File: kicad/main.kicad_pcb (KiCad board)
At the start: 2 copper layers, 198.1 x 99.1 mm, 66 parts, among them J1 Jack-DC, J12 I2C1, J14 LCD_Conn, J15 VIA_A, J2 UART, J3 Data, J4 PWR, J5 uSD, J6 VIA_B, J7 IO~{EN}_{[3..7]}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

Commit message: WIP: V16 GAL stuff
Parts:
- removed J6: VIA_B, Connector_PinHeader_2.54mm:PinHeader_1x04_P2.54mm_Vertical
- J2: footprint Connector_PinHeader_2.54mm:PinHeader_1x04_P2.54mm_Horizontal -> Connector_PinHeader_2.54mm:PinHeader_1x04_P2.54mm_Vertical
- J7: value IO~{EN}_{[3..7]} -> IO~{EN}_{[3..4]}; footprint Connector_PinHeader_2.54mm:PinHeader_1x05_P2.54mm_Vertical -> Connector_PinHeader_2.54mm:PinHeader_1x02_P2.54mm_Vertical
- moved R10 71.5 mm to (121.9, 61.0), turned to 180 degrees
- moved R11 68.6 mm to (121.9, 66.0), turned to 180 degrees
- moved C8 64.4 mm to (101.2, 113.5), turned to 90 degrees
- moved D3 29.0 mm to (190.5, 94.0)
- moved ROM1 27.4 mm to (57.6, 115.4), turned to 90 degrees
- moved J3 24.1 mm to (165.1, 106.7)
- moved X2 17.0 mm to (27.9, 78.7), turned to 90 degrees
- moved J4 10.5 mm to (182.9, 96.5)
- moved J7 5.68 mm to (165.1, 94.0)
- moved U4 5.08 mm to (176.5, 39.4)
- moved Y1 5.08 mm to (176.1, 34.0)
- moved J8 3.59 mm to (139.7, 94.0)
- moved C3 3.59 mm to (167.6, 77.5)
- moved IO1 3.59 mm to (154.9, 81.3)
- moved J9 2.54 mm to (139.7, 106.7)
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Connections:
- IO1 pad 10: IO~{EN}_{5} -> unconnected-(IO1-O5-Pad10)
- IO1 pad 7: IO~{EN}_{7} -> unconnected-(IO1-O7-Pad7)
- IO1 pad 9: IO~{EN}_{6} -> unconnected-(IO1-O6-Pad9)
- U6 pad 9: unconnected-(U6-I9-Pad9) -> ~{RES}
- VIA1 pad 17: Net-(J6-Pin_3) -> unconnected-(VIA1-PB7-Pad17)
- VIA1 pad 18: Net-(J6-Pin_4) -> unconnected-(VIA1-CB1-Pad18)
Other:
- board text added: "IO~EN~[3..4]"
- board text added: "by Andrew Dunai & 6502.org community"
- board text added: "m6502 SBC"
- board text removed: "65ad02"
- board text removed: "IO~EN~[2..7]"
- board text removed: "VIA_B"
- board text removed: "by and3rson & 6502.org community"

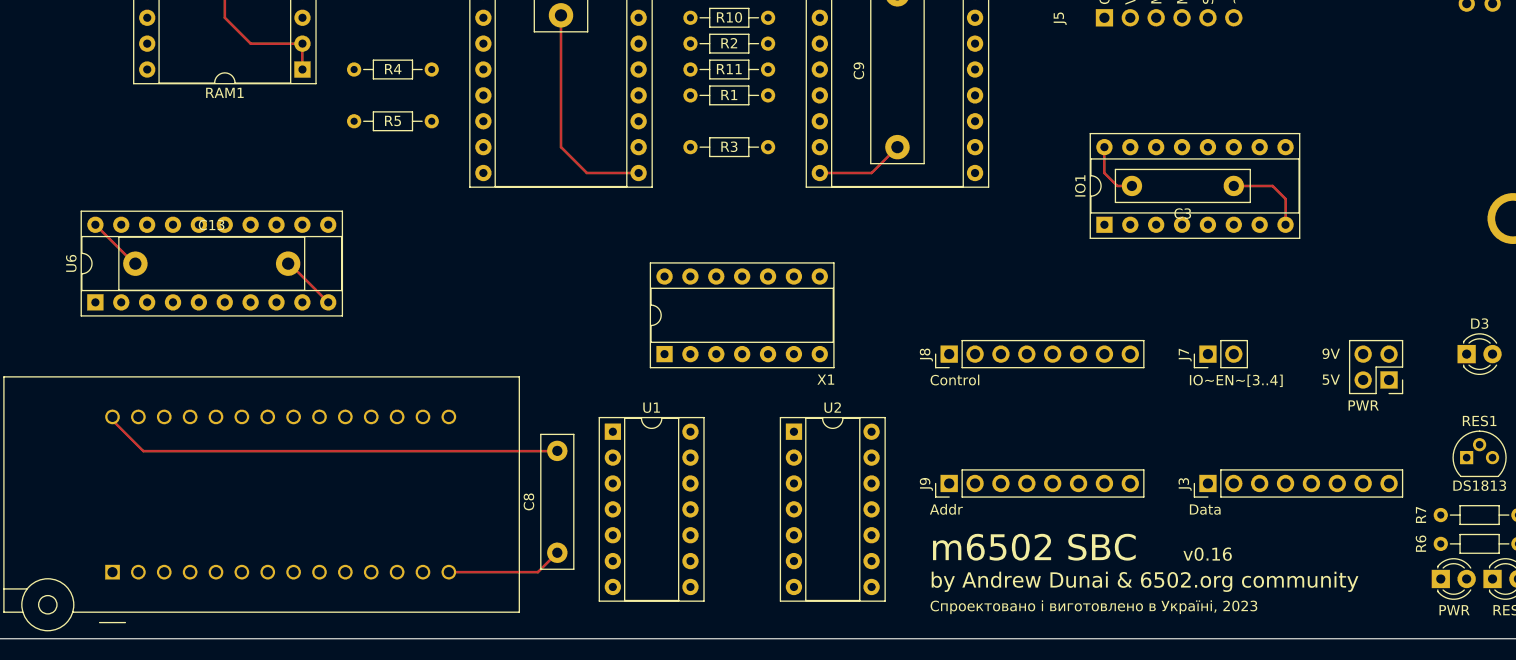
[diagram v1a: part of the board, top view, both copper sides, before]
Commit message: Replace address decoder & r/w qualifier with GAL
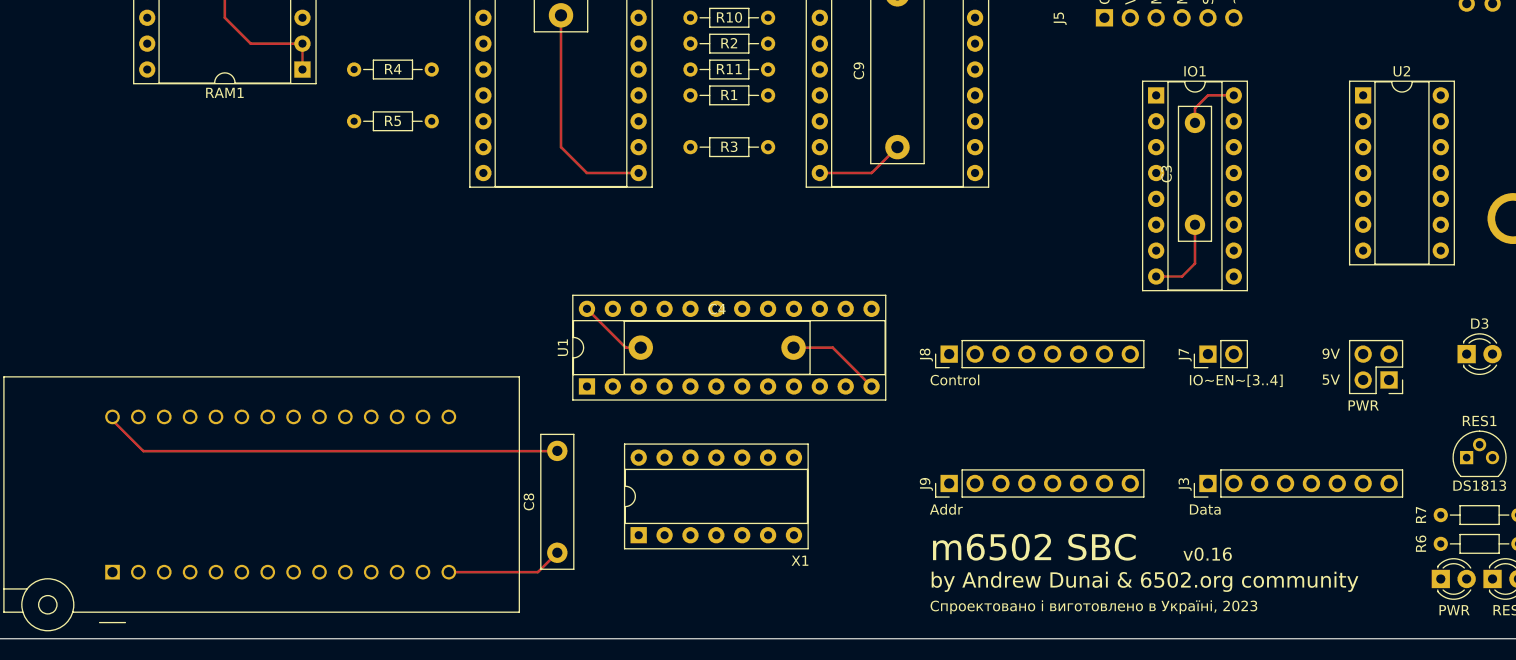
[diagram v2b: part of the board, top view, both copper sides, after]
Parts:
- removed C13: 0.1uF, Capacitor_THT:C_Rect_L18.0mm_W5.0mm_P15.00mm_FKS3_FKP3
- removed U6: GAL16V8, Package_DIP:DIP-20_W7.62mm_Socket
- added C4: 0.1uF, Capacitor_THT:C_Rect_L18.0mm_W5.0mm_P15.00mm_FKS3_FKP3, F.Cu at (109.4, 93.3)
- U1: value 74HC00 -> GAL20V8; footprint Package_DIP:DIP-14_W7.62mm_Socket -> Package_DIP:DIP-24_W7.62mm_Socket
- moved U2 64.9 mm to (180.3, 68.6)
- moved X1 18.0 mm to (109.2, 111.8)
- moved IO1 13.7 mm to (160.0, 68.6), turned to 0 degrees
- moved C3 5.39 mm to (163.8, 81.3), turned to 90 degrees
- moved U1 5.12 mm to (104.1, 97.2), turned to 90 degrees
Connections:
- IO1 pad 4: A_{13} -> GND
- IO1 pad 5: Net-(IO1-E2) -> IO~{EN}
- IO1 pad 6: A_{12} -> +5V
- U1 pad 1: A_{13} -> CLK
- U1 pad 10: A_{15} -> unconnected-(U1-I-Pad10)
- U1 pad 11: Net-(IO1-E2) -> unconnected-(U1-I-Pad11)
- U1 pad 12: A_{14} -> GND
- U1 pad 13: A_{15} -> GND
- U1 pad 14: +5V -> unconnected-(U1-I-Pad14)
- U1 pad 2: A_{14} -> unconnected-(U1-I-Pad2)
- U1 pad 3: Net-(U1-Pad3) -> LCD~{EN}
- U1 pad 4: Net-(U1-Pad3) -> ~{RES}
- U1 pad 5: A_{14} -> A_{12}
- U1 pad 6: Net-(U1-Pad6) -> A_{13}
- U1 pad 7: GND -> A_{14}
- U1 pad 8: ROM~{EN} -> A_{15}
- U1 pad 9: Net-(U1-Pad6) -> R~{W}
- U2 pad 1: R~{W} -> ~{RES}
- U2 pad 10: R~{W} -> (no net)
- U2 pad 11: Net-(R7-Pad1) -> (no net)
- U2 pad 12: ~{RES} -> (no net)
- U2 pad 13: ~{RES} -> (no net)
- U2 pad 2: R~{W} -> ~{RES}
- U2 pad 3: Net-(U2-Pad3) -> Net-(R7-Pad1)
- U2 pad 4: Net-(U2-Pad3) -> (no net)
- U2 pad 5: Ф2 -> (no net)
- U2 pad 6: ~{WD} -> (no net)
- U2 pad 8: ~{RD} -> (no net)
- U2 pad 9: Ф2 -> (no net)
- X1 pad 8: Net-(U6-I1/CLK) -> CLK
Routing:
- net GND: track 114.0 -> 117.7 mm
- net +5V: track 108.0 -> 109.3 mm

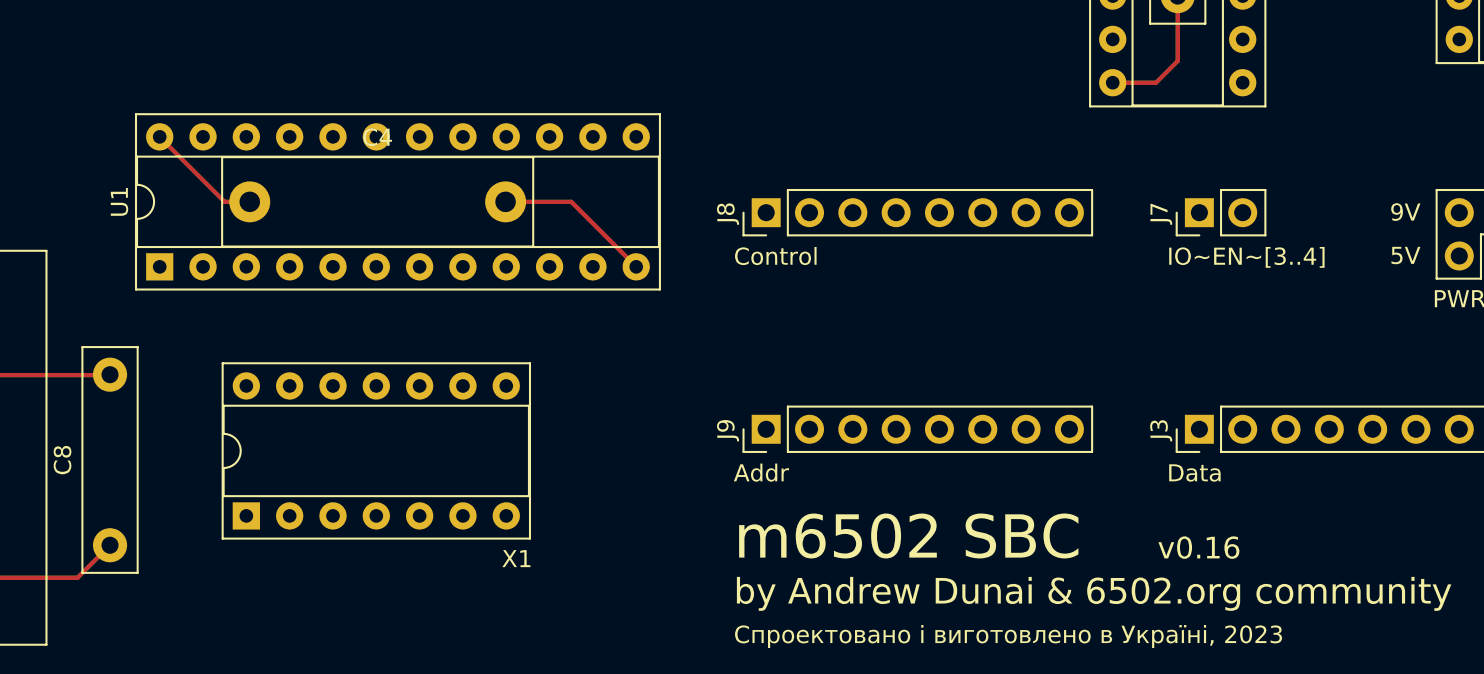
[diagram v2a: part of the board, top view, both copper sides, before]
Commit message: Replace GAL20V8 with GAL(ATF)16V8
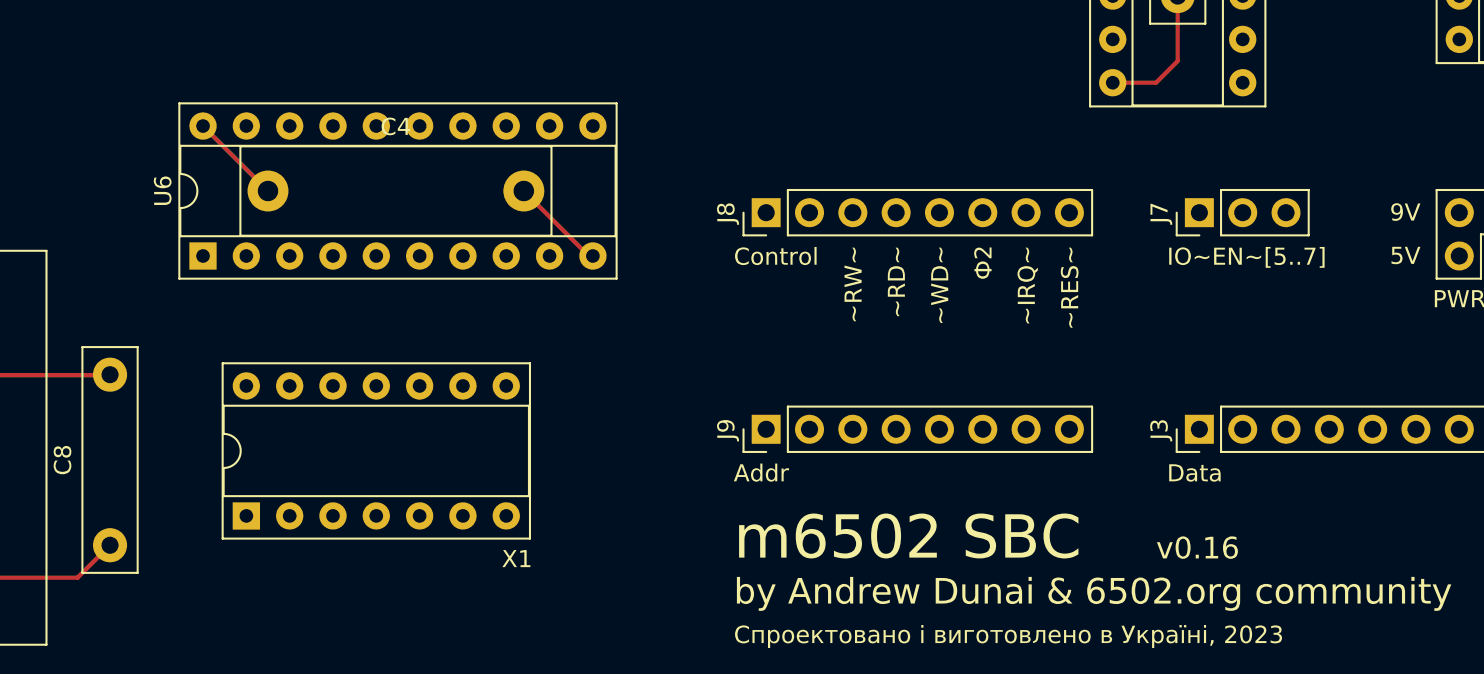
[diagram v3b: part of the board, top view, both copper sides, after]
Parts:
- removed U1: GAL20V8, Package_DIP:DIP-24_W7.62mm_Socket
- added U6: ATF16V8B-15PU, Package_DIP:DIP-20_W7.62mm_Socket, F.Cu at (106.7, 96.5)
- J7: value IO~{EN}_{[3..4]} -> IO~{EN}_{[5..7]}; footprint Connector_PinHeader_2.54mm:PinHeader_1x02_P2.54mm_Vertical -> Connector_PinHeader_2.54mm:PinHeader_1x03_P2.54mm_Vertical
- moved C4 1.24 mm to (110.5, 92.7)
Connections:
- IO1 pad 10: unconnected-(IO1-O5-Pad10) -> IO~{EN}_{5}
- IO1 pad 11: IO~{EN}_{4} -> SID~{EN}
- IO1 pad 12: IO~{EN}_{3} -> unconnected-(IO1-O3-Pad12)
- IO1 pad 7: unconnected-(IO1-O7-Pad7) -> IO~{EN}_{7}
- IO1 pad 9: unconnected-(IO1-O6-Pad9) -> IO~{EN}_{6}
- J7 pad 1: IO~{EN}_{3} -> IO~{EN}_{5}
- J7 pad 2: IO~{EN}_{4} -> IO~{EN}_{6}
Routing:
- net GND: track 117.7 -> 114.1 mm
- net +5V: track 109.3 -> 107.8 mm
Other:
- board text added: "IO~EN~[5..7]"
- board text added: "~IRQ~"
- board text added: "~RD~"
- board text added: "~RES~"
- board text added: "~RW~"
- board text added: "~WD~"
- board text added: "Ф2"
- board text removed: "IO~EN~[3..4]"

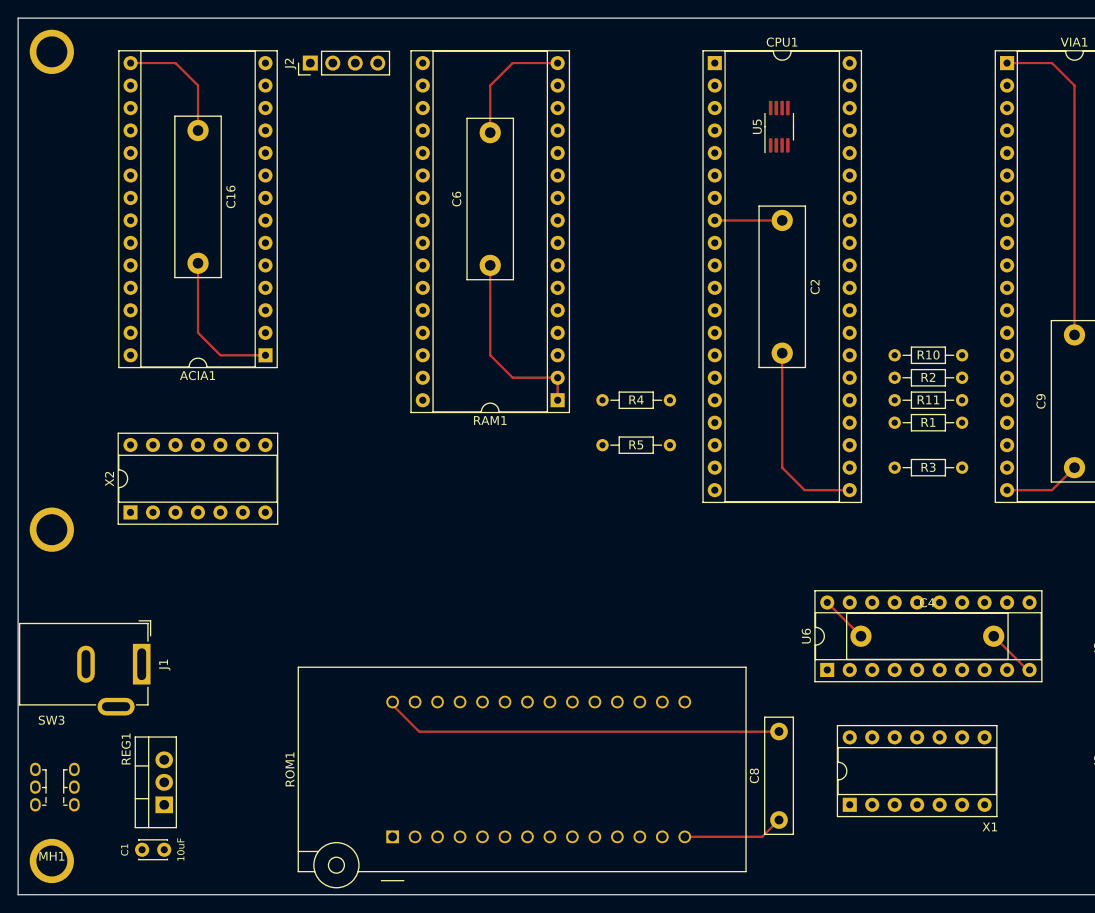
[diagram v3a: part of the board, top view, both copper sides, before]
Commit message: Move power socket to top, move GAL down a bit
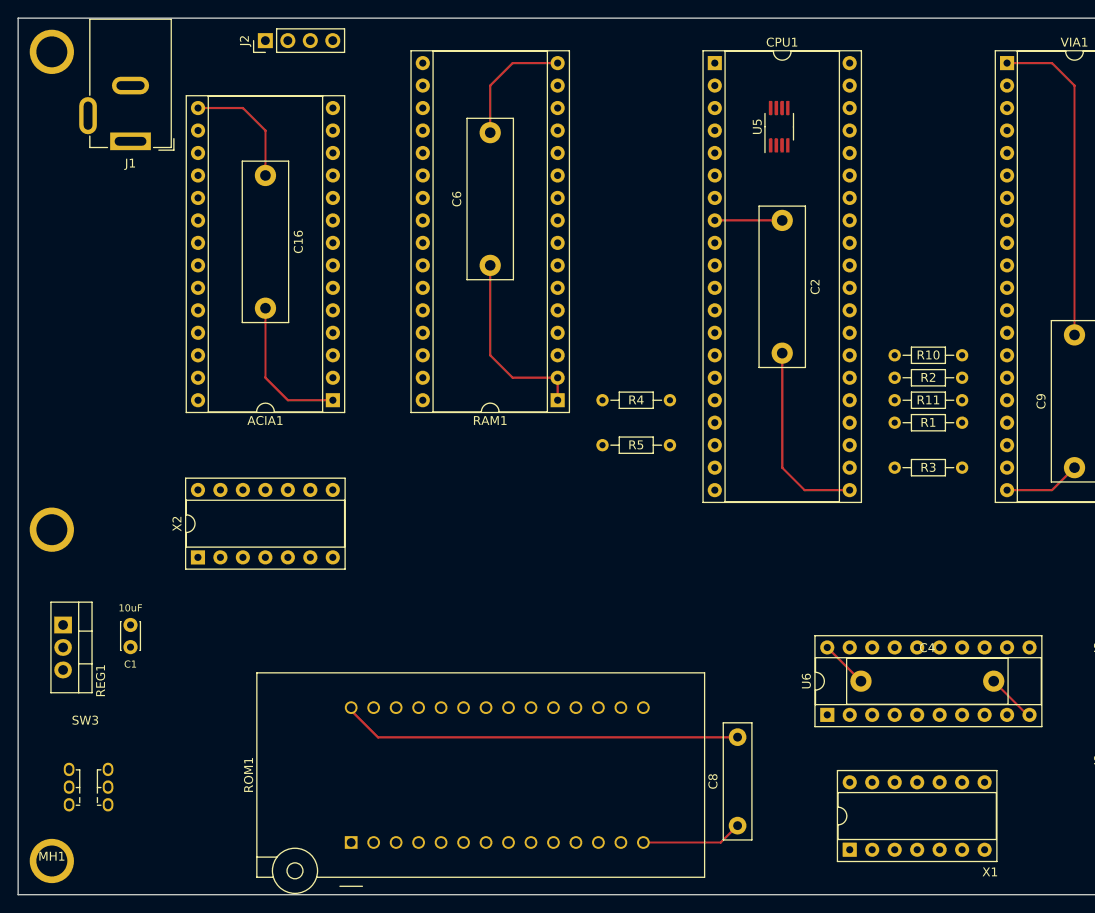
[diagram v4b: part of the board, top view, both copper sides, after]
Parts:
- moved J1 59.1 mm to (27.9, 36.8), turned to 180 degrees
- moved C1 25.7 mm to (27.9, 91.4), turned to -90 degrees
- moved REG1 23.3 mm to (20.3, 91.4), turned to -90 degrees
- moved ACIA1 9.16 mm to (50.8, 66.0)
- moved X2 9.16 mm to (35.6, 83.8)
- moved C16 9.16 mm to (43.2, 40.6)
- moved J2 5.68 mm to (43.2, 25.4)
- moved C4 5.08 mm to (110.5, 97.8)
- moved U6 5.08 mm to (106.7, 101.6)
- moved X1 5.08 mm to (109.2, 116.8)
- moved C8 4.73 mm to (96.5, 114.1)
- moved ROM1 4.73 mm to (52.9, 116.0)
- moved SW3 3.81 mm to (20.3, 106.9)
